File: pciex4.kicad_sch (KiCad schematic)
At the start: 0 parts

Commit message: finished the pciex4 implememntation
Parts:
- added C1, C2, C3, C4, C5, C6, C7, C8: 220nF/50v, A_HDJ_Library:C_0402_1005Metric, symbol Device:C_Small
- added C10, C13, C15, C9: 100nF/50V, A_HDJ_Library:C_0402_1005Metric, symbol Device:C
- added C11: 100uF/100v, A_HDJ_Library:CP_Elec_6.3x7.7, symbol Device:C_Polarized
- added C14: 10uF/10V, A_HDJ_Library:C_0402_1005Metric, symbol Device:C
- added C16: 560uF/25V, A_HDJ_Library:CP_Elec_6.3x7.7, symbol Device:C_Polarized
- added J79: Bus_PCI_Express_x4, A_HDJ_Library:PCIe_x4_Gen3Slot_Connectors, symbol Connector:Bus_PCI_Express_x4
- added TP1: TestPoint, symbol Connector:TestPoint
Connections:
- new net: C10.1, C11.1, C9.1, J79.A2 (+12V), J79.A3 (+12V), J79.B1 (+12V), J79.B2 (+12V), J79.B3 (+12V)
- new net +3.3V: C13.2, C14.2, C15.1, C16.1, J79.A10 (+3.3V), J79.A9 (+3.3V), J79.B10 (3.3Vaux), J79.B8 (+3.3V)
- new net GND: C10.2, C11.2, C15.2, C16.2, C9.2, J79.A1 (~{PRSNT1}), J79.A12 (GND), J79.A15 (GND), J79.A18 (GND), J79.A20 (GND), J79.A23 (GND), J79.A24 (GND), J79.A27 (GND), J79.A28 (GND), J79.A31 (GND), J79.A4 (GND), J79.B13 (GND), J79.B16 (GND), J79.B17 (~{PRSNT2}), J79.B18 (GND), J79.B21 (GND), J79.B22 (GND), J79.B25 (GND), J79.B26 (GND), J79.B29 (GND), J79.B31 (~{PRSNT2}), J79.B32 (GND), J79.B4 (GND), J79.B7 (GND)
- new net PCIe30_TX0_N: C2.2, J79.B15 (PETn0)
- new net PCIe30_TX0_P: C1.2, J79.B14 (PETp0)
- new net PCIe30_TX1_N: C4.2, J79.B20 (PETn1)
- new net PCIe30_TX1_P: C3.2, J79.B19 (PETp1)
- new net PCIe30_TX2_N: C6.2, J79.B24 (PETn2)
- new net PCIe30_TX2_P: C5.2, J79.B23 (PETp2)
- new net PCIe30_TX3_N: C8.2, J79.B28 (PETn3)
- new net PCIe30_TX3_P: C7.2, J79.B27 (PETp3)
- new net PCIe_RX_0+: J79.A16 (PERp0)
- new net PCIe_RX_0-: J79.A17 (PERn0)
- new net PCIe_RX_1+: J79.A21 (PERp1)
- new net PCIe_RX_1-: J79.A22 (PERn1)
- new net PCIe_RX_2+: J79.A25 (PERp2)
- new net PCIe_RX_2-: J79.A26 (PERn2)
- new net PCIe_RX_3+: J79.A29 (PERp3)
- new net PCIe_RX_3-: J79.A30 (PERn3)
- new net PCIe_TX_0+: C1.1
- new net PCIe_TX_0-: C2.1
- new net PCIe_TX_1+: C3.1
- new net PCIe_TX_1-: C4.1
- new net PCIe_TX_2+: C5.1
- new net PCIe_TX_2-: C6.1
- new net PCIe_TX_3+: C7.1
- new net PCIe_TX_3-: C8.1
- new net REFCLK+: J79.A13 (REFCLK+)
- new net REFCLK-: J79.A14 (REFCLK-)
- new net ~{PE_RST}: J79.A11 (~{PERST}), TP1.1
- new net ~{WAKE}: J79.B11 (~{WAKE})
- no-connect marks 0 -> 5

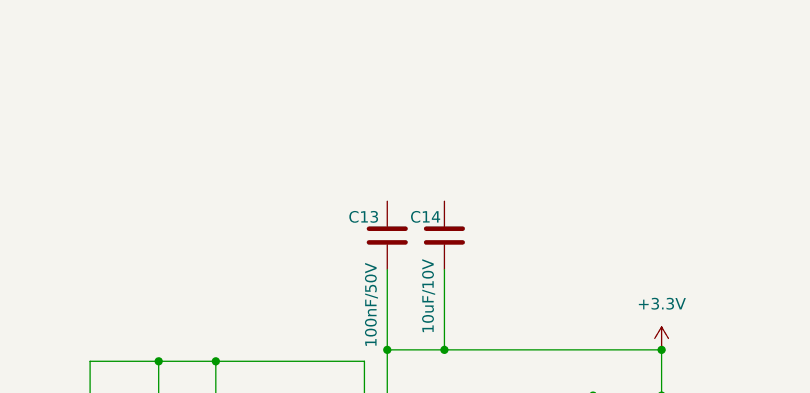
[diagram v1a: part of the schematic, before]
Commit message: Connected the hierchal labels to the main mu module in the root sheet
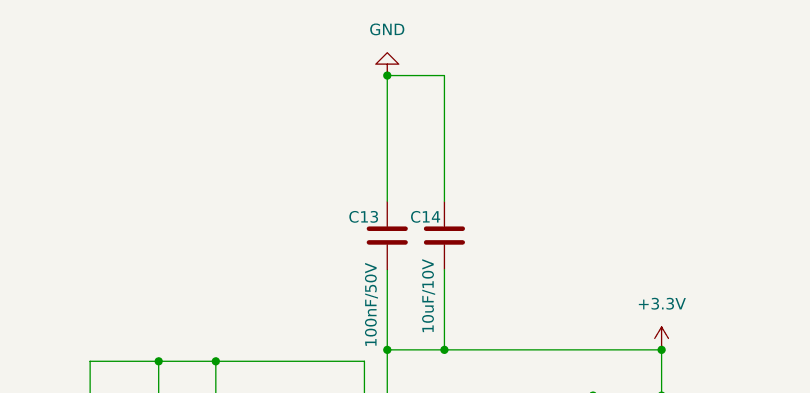
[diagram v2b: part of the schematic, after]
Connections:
- net GND: now also C13.1, C14.1
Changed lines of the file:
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@@
 	(paper "A4")
+	(junction
+		(at 139.7 31.75)
+		(diameter 0)
+		(color 0 0 0 0)
+	)
 	(junction
 		(at 114.3 63.5)
@@
 	(wire
 		(pts
+			(xy 146.05 31.75) (xy 139.7 31.75)
+		)
+		(stroke
+			(width 0)
+			(type default)
+		)
+	)
+	(wire
+		(pts
 			(xy 114.3 78.74) (xy 114.3 83.82)
 		)
@@
 	(wire
 		(pts
+			(xy 146.05 45.72) (xy 146.05 31.75)
+		)
+		(stroke
+			(width 0)
+			(type default)
+		)
+	)
+	(wire
+		(pts
 			(xy 114.3 63.5) (xy 114.3 71.12)
 		)
@@
 		(pts
 			(xy 104.14 135.89) (xy 124.46 135.89)
+		)
+		(stroke
+			(width 0)
+			(type default)
+		)
+	)
+	(wire
+		(pts
+			(xy 139.7 31.75) (xy 139.7 45.72)
 		)
 		(stroke
@@
 					(unit 1)
 				)
+			)
+		)
+	)
+	(symbol
+		(lib_id "power:GND")
+		(at 139.7 31.75 180)
+		(unit 1)
+		(body_style 1)
+		(exclude_from_sim no)
+		(in_bom yes)
+		(on_board yes)
+		(in_pos_files yes)
+		(dnp no)
+		(fields_autoplaced yes)
+		(property "Reference" "#PWR0150"
+			(at 139.7 25.4 0)
+			(hide yes)
+			(show_name no)
+			(do_not_autoplace no)
+			(effects
+				(font
+					(size 1.27 1.27)
+				)
+			)
+		)
+		(property "Value" "GND"
+			(at 139.7 26.67 0)
+			(show_name no)
+			(do_not_autoplace no)
+			(effects
+				(font
+					(size 1.27 1.27)
+				)
+			)
+		)
+		(property "Footprint" ""
+			(at 139.7 31.75 0)
+			(hide yes)
+			(show_name no)
+			(do_not_autoplace no)
+			(effects
+				(font
+					(size 1.27 1.27)
+				)
+			)
+		)
+		(property "Datasheet" ""
+			(at 139.7 31.75 0)
+			(hide yes)
+			(show_name no)
+			(do_not_autoplace no)
+			(effects
+				(font
+					(size 1.27 1.27)
+				)
+			)
+		)
+		(property "Description" "Power symbol creates a global label with name \"GND\" , ground"
+			(at 139.7 31.75 0)
+			(hide yes)
+			(show_name no)
+			(do_not_autoplace no)
+			(effects
+				(font
+					(size 1.27 1.27)
+				)
+			)
+		)
+		(pin "1"
+		)
+		(instances
+			(project "Carrier_Board"
+				(path "/e768274e-12f3-4f83-96f6-abb7638e0bc1/d05d8b94-71f3-437a-a0af-11ed4e3069d0"
+					(reference "#PWR0150")
+					(unit 1)
+				)

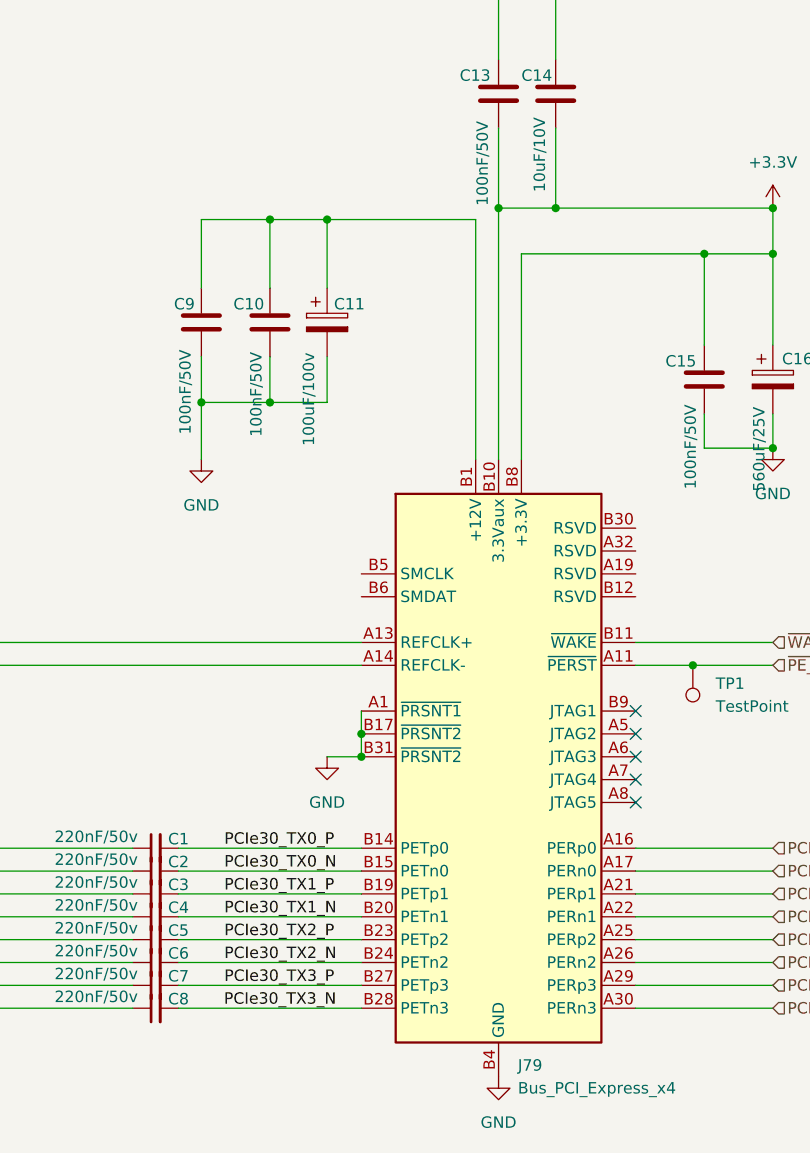
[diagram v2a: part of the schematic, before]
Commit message: Fixed annotation errors duplicate designators on passive components R11 and J15 so that schematic could be imported into pcb. There might be some missing footprints... starting that investigation
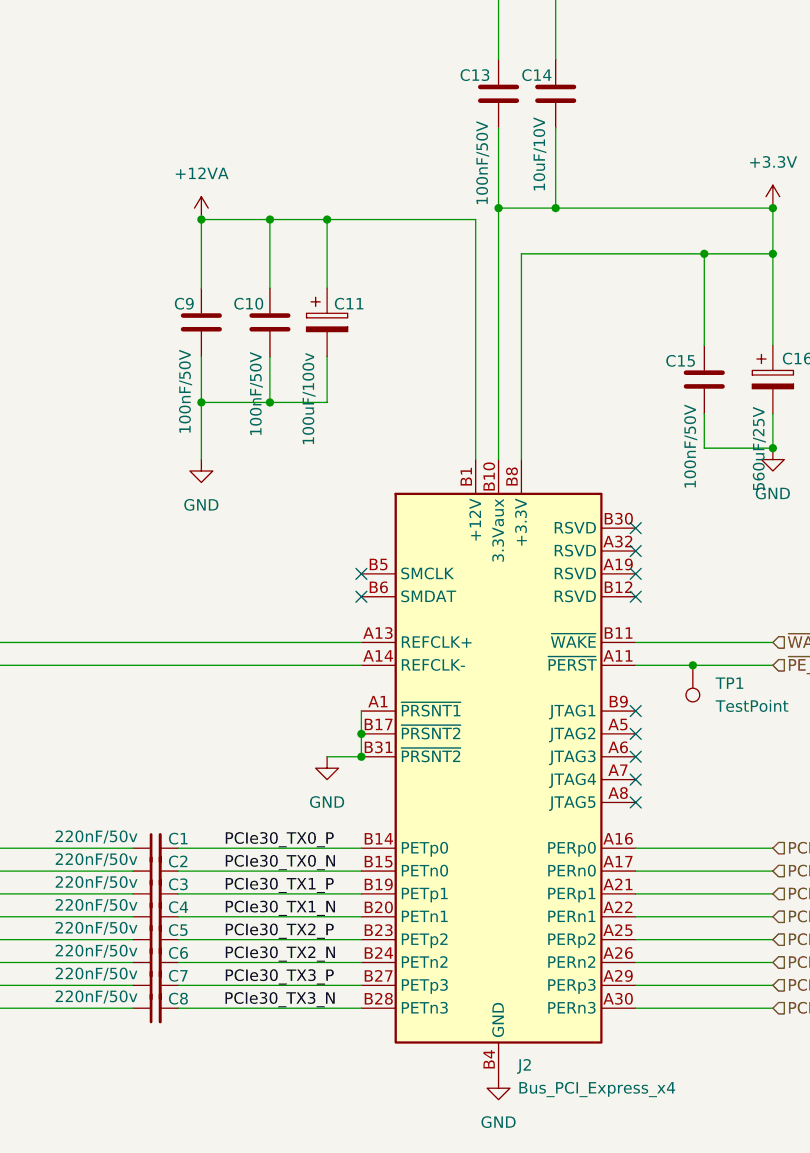
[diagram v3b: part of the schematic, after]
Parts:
- renumbered J79 to J2
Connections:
- net +12VA: now reaches C10.1, C11.1, C9.1, J2.A2 (+12V), J2.A3 (+12V), J2.B1 (+12V), J2.B2 (+12V), J2.B3 (+12V)
- no-connect marks 5 -> 11
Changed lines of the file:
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@@
+	)
+	(junction
+		(at 106.68 63.5)
+		(diameter 0)
+		(color 0 0 0 0)
 	)
 	(junction
@@
 	)
 	(no_connect
+		(at 154.94 105.41)
+	)
+	(no_connect
 		(at 154.94 128.27)
+	)
+	(no_connect
+		(at 154.94 102.87)
 	)
 	(no_connect
@@
 	)
 	(no_connect
+		(at 124.46 102.87)
+	)
+	(no_connect
+		(at 154.94 97.79)
+	)
+	(no_connect
 		(at 154.94 125.73)
+	)
+	(no_connect
+		(at 154.94 100.33)
 	)
 	(no_connect
@@
 	(no_connect
 		(at 154.94 120.65)
+	)
+	(no_connect
+		(at 124.46 105.41)
 	)
 	(wire
@@
 		(dnp no)
 		(fields_autoplaced yes)
-		(property "Reference" "J79"
+		(property "Reference" "J2"
 			(at 141.8433 157.48 0)
 			(show_name no)
@@
 			(project "Carrier_Board"
 				(path "/e768274e-12f3-4f83-96f6-abb7638e0bc1/d05d8b94-71f3-437a-a0af-11ed4e3069d0"
-					(reference "J79")
+					(reference "J2")
 					(unit 1)
 				)
+			)
+		)
+	)
+	(symbol
+		(lib_id "power:+12VA")
+		(at 106.68 63.5 0)
+		(unit 1)
+		(body_style 1)
+		(exclude_from_sim no)
+		(in_bom yes)
+		(on_board yes)
+		(in_pos_files yes)
+		(dnp no)
+		(fields_autoplaced yes)
+		(property "Reference" "#PWR0200"
+			(at 106.68 67.31 0)
+			(hide yes)
+			(show_name no)
+			(do_not_autoplace no)
+			(effects
+				(font
+					(size 1.27 1.27)
+				)
+			)
+		)
+		(property "Value" "+12VA"
+			(at 106.68 58.42 0)
+			(show_name no)
+			(do_not_autoplace no)
+			(effects
+				(font
+					(size 1.27 1.27)
+				)
+			)
+		)
+		(property "Footprint" ""
+			(at 106.68 63.5 0)
+			(hide yes)
+			(show_name no)
+			(do_not_autoplace no)
+			(effects
+				(font
+					(size 1.27 1.27)
+				)
+			)
+		)
+		(property "Datasheet" ""
+			(at 106.68 63.5 0)
+			(hide yes)
+			(show_name no)
+			(do_not_autoplace no)
+			(effects
+				(font
+					(size 1.27 1.27)
+				)
+			)
+		)
+		(property "Description" "Power symbol creates a global label with name \"+12VA\""
+			(at 106.68 63.5 0)
+			(hide yes)
+			(show_name no)
+			(do_not_autoplace no)
+			(effects
+				(font
+					(size 1.27 1.27)
+				)
+			)
+		)
+		(pin "1"
+		)
+		(instances
+			(project "Carrier_Board"
+				(path "/e768274e-12f3-4f83-96f6-abb7638e0bc1/d05d8b94-71f3-437a-a0af-11ed4e3069d0"
+					(reference "#PWR0200")
+					(unit 1)
+				)
